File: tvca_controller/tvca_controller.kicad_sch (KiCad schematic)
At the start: 22 parts, among them J1 Programming Header, J2 CAN connector, J3 Batt, J8 Batt, U1 PIC18F26K83, U2 MCP2562, U3 INA180, Y1 Crystal

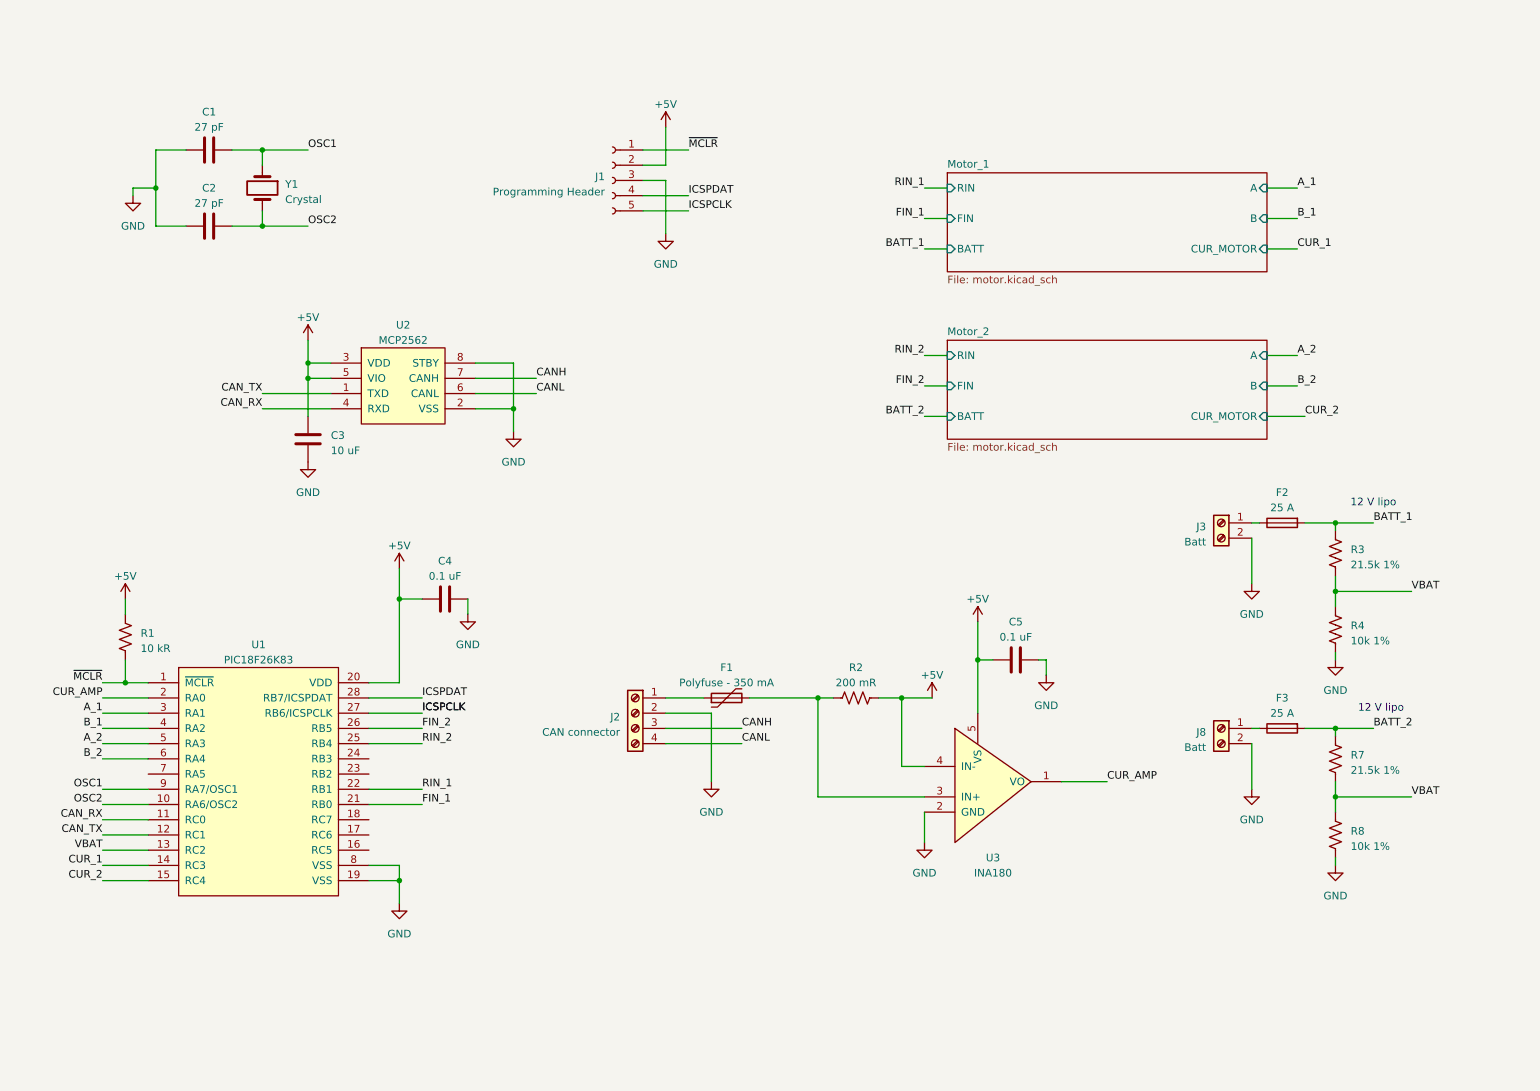
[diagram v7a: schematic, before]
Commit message: Finish up schematic for jack to review, start PCB layout
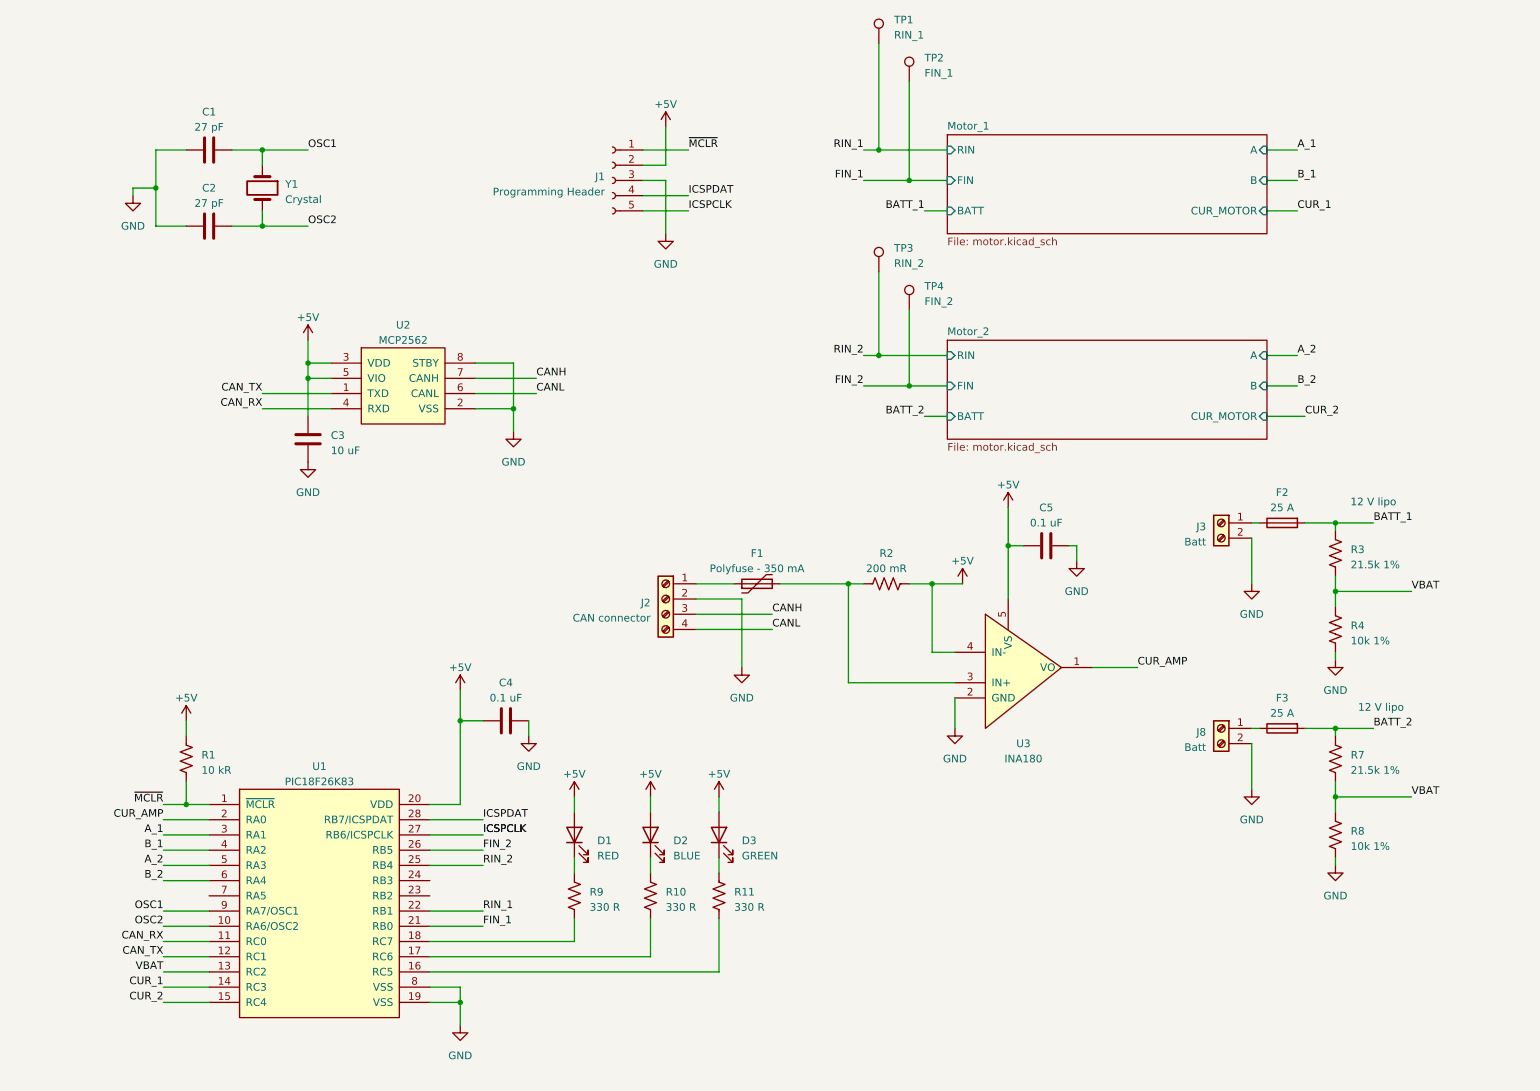
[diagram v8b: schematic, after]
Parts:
- added D1: RED, LED_SMD:LED_0805_2012Metric_Pad1.15x1.40mm_HandSolder, symbol Device:LED
- added D2: BLUE, LED_SMD:LED_0805_2012Metric_Pad1.15x1.40mm_HandSolder, symbol Device:LED
- added D3: GREEN, LED_SMD:LED_0805_2012Metric_Pad1.15x1.40mm_HandSolder, symbol Device:LED
- added R10, R11, R9: 330 R, Resistor_SMD:R_0805_2012Metric_Pad1.20x1.40mm_HandSolder, symbol Device:R_US
- added TP1: RIN_1, TestPoint:TestPoint_THTPad_2.5x2.5mm_Drill1.2mm, symbol Connector:TestPoint
- added TP2: FIN_1, TestPoint:TestPoint_THTPad_2.5x2.5mm_Drill1.2mm, symbol Connector:TestPoint
- added TP3: RIN_2, TestPoint:TestPoint_THTPad_2.5x2.5mm_Drill1.2mm, symbol Connector:TestPoint
- added TP4: FIN_2, TestPoint:TestPoint_THTPad_2.5x2.5mm_Drill1.2mm, symbol Connector:TestPoint
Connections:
- net +5V: now also D1.2 (A), D2.2 (A), D3.2 (A)
- net FIN_1: now also TP2.1
- net FIN_2: now also TP4.1
- net RIN_1: now also TP1.1
- net RIN_2: now also TP3.1
- net at U1.16 (RC5): now also R11.1
- net at U1.17 (RC6): now also R10.1
- net at U1.18 (RC7): now also R9.1
- new net: D1.1 (K), R9.2
- new net: D3.1 (K), R11.2
- new net: D2.1 (K), R10.2
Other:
- moved on the sheet: C4, C5, F1, J2, R1, R2, U1, U3
